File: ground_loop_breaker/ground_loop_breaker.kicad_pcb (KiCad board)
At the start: 2 copper layers, 72 parts, among them J1 Conn_01x02_Male, J10 Conn_01x02_Male, J11 Conn_Coaxial, J12 Conn_01x02_Male, J2 Conn_01x02_Male, J3 Conn_Coaxial, J4 Conn_01x02_Male, J5 Conn_Coaxial, J6 Conn_01x02_Male, J7 Conn_01x02_Male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

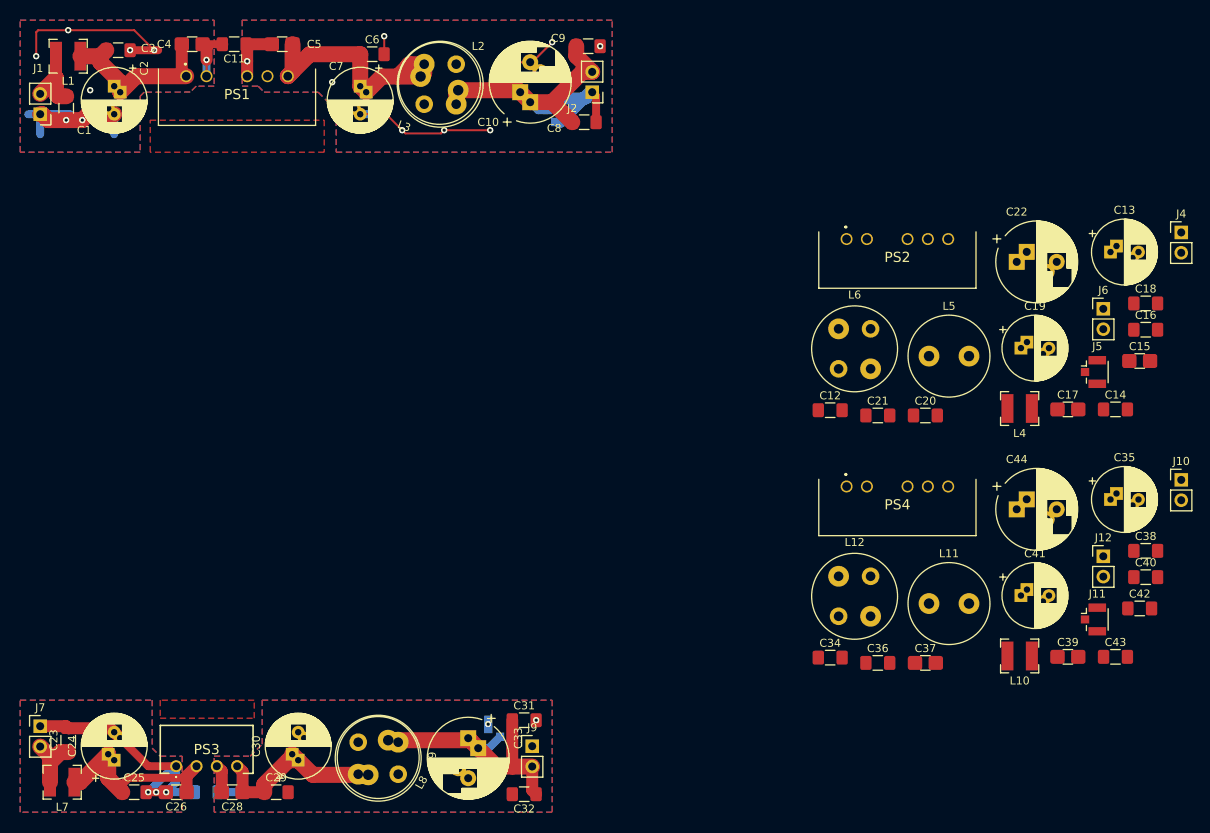
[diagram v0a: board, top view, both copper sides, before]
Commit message: ground loop breaker fin
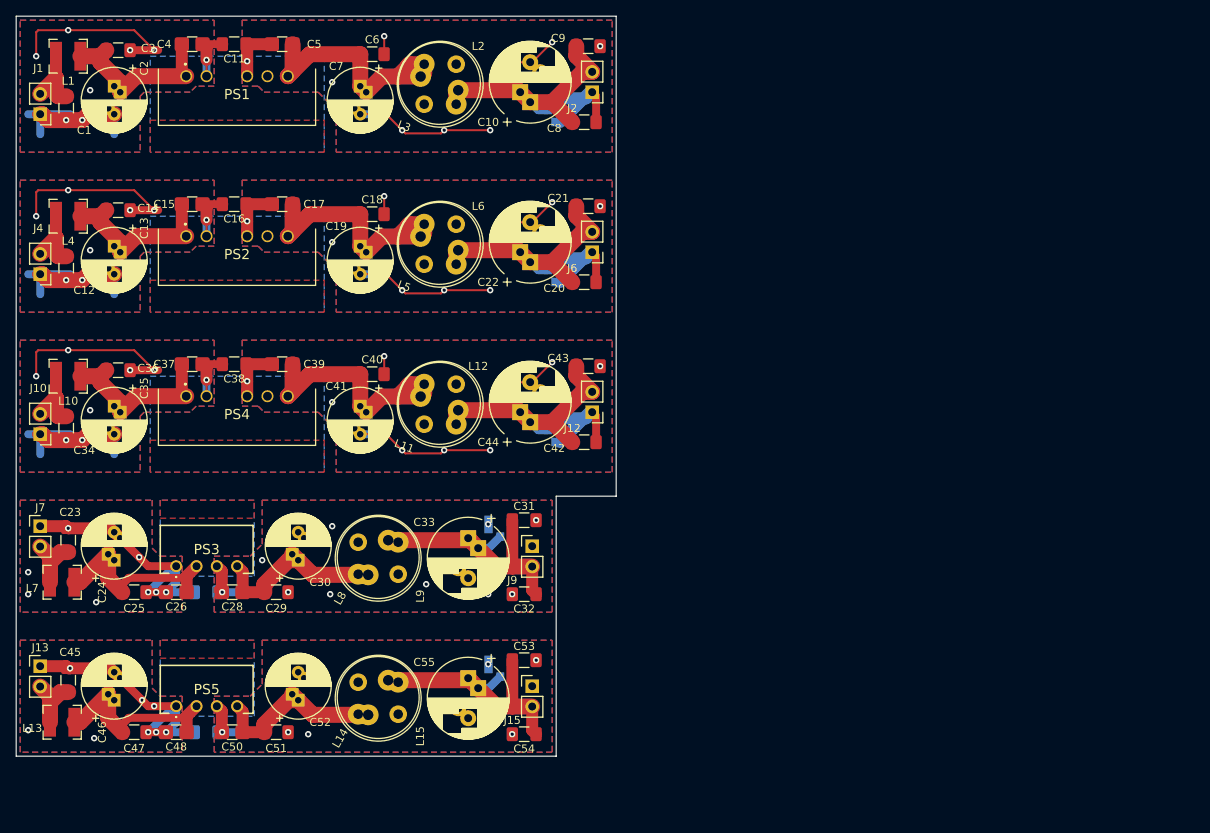
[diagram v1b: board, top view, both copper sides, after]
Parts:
- added C45: C, Capacitor_SMD:C_1206_3216Metric_Pad1.42x1.75mm_HandSolder, F.Cu at (81.5, 133.0)
- added C46: CP, SamacSys_Parts:CP_Radial_D8_P3.5_2.5, F.Cu at (87.2, 135.5)
- added C47: C, Capacitor_SMD:C_1206_3216Metric_Pad1.42x1.75mm_HandSolder, F.Cu at (89.8, 139.5)
- added C48: C, SamacSys_Parts:C_1206_0805_dual, F.Cu at (95.0, 139.5)
- added C49: 270p 1kV, Capacitor_SMD:C_1206_3216Metric_Pad1.42x1.75mm_HandSolder, B.Cu at (98.8, 139.5)
- added C50: C, SamacSys_Parts:C_1206_0805_dual, F.Cu at (102.0, 139.5)
- added C51: C, Capacitor_SMD:C_1206_3216Metric_Pad1.42x1.75mm_HandSolder, F.Cu at (107.5, 139.5)
- added C52: CP, SamacSys_Parts:CP_Radial_D8_P3.5_2.5, F.Cu at (110.2, 135.5)
- added C53: C, Capacitor_SMD:C_1206_3216Metric_Pad1.42x1.75mm_HandSolder, F.Cu at (138.5, 130.5)
- added C54: C, Capacitor_SMD:C_1206_3216Metric_Pad1.42x1.75mm_HandSolder, F.Cu at (138.5, 139.8)
- added C55: CP, SamacSys_Parts:CP_Radial_D10.0mm_P3.5_5, F.Cu at (131.5, 132.8)
- added J13: Conn_01x02_Male, Connector_PinHeader_2.54mm:PinHeader_1x02_P2.54mm_Vertical, F.Cu at (78.0, 131.2)
- added J14: Conn_Coaxial, Connector_Coaxial:U.FL_Hirose_U.FL-R-SMT-1_Vertical, B.Cu at (135.5, 131.5)
- added J15: Conn_01x02_Male, Connector_PinHeader_2.54mm:PinHeader_1x02_P2.54mm_Vertical, F.Cu at (139.5, 133.8)
- added L13: L, Inductor_SMD:L_Bourns-SRN4018, F.Cu at (80.8, 138.2)
- added L14: 12RS105C, Inductor_THT:L_Radial_D10.0mm_P5.00mm_Fastron_07P, F.Cu at (121.5, 133.0)
- added L15: 12RS105C, Inductor_THT:L_Radial_D10.5mm_P4.00x5.00mm_Murata_1200RS, F.Cu at (122.8, 133.2)
- added PS5: PDSE1-S5-S5-S, SamacSys_Parts:PDSE1S5S5S, F.Cu at (95.0, 136.2)
- J11, J5: moved to B.Cu
- moved J10 142.7 mm to (78.0, 102.2), turned to 180 degrees
- moved J4 142.7 mm to (78.0, 82.2), turned to 180 degrees
- moved C14 127.1 mm to (87.8, 74.2)
- moved C35 125.1 mm to (87.2, 98.8), turned to 270 degrees
- moved C13 124.5 mm to (87.2, 78.8), turned to 270 degrees
- moved L10 124.0 mm to (81.5, 95.0)
- moved L4 121.3 mm to (81.5, 75.0)
- moved C15 120.1 mm to (97.0, 73.5)
- moved C38 116.3 mm to (102.2, 93.5), turned to 180 degrees
- moved C16 115.0 mm to (102.2, 73.5), turned to 180 degrees
- moved C39 104.8 mm to (108.2, 93.5), turned to 180 degrees
- moved C36 101.8 mm to (87.8, 94.2)
- moved C17 101.5 mm to (108.2, 73.5), turned to 180 degrees
- moved C40 100.0 mm to (119.5, 94.8)
- moved C34 99.7 mm to (81.2, 101.5), turned to 270 degrees
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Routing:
- net /sheet61358710/VinN: track 0.00 -> 55.2 mm, vias 0 -> 8
- net /sheet613586DC/VinN: track 0.00 -> 55.2 mm, vias 0 -> 8
- net /sheet61358710/VoutN: track 0.00 -> 52.5 mm, vias 0 -> 9
- net /sheet613586DC/VoutN: track 0.00 -> 52.5 mm, vias 0 -> 9
- net /sheet61365BC2/VinN: track 0.00 -> 33.7 mm, vias 0 -> 9
- net /sheet61365BC2/VoutP: track 0.00 -> 33.5 mm
- net Net-(C39-Pad1): track 0.00 -> 32.8 mm
- net Net-(C17-Pad1): track 0.00 -> 32.8 mm
- net /sheet61358710/VoutP: track 0.00 -> 31.0 mm
- net /sheet613586DC/VoutP: track 0.00 -> 31.0 mm
- net Net-(C50-Pad1): track 0.00 -> 24.8 mm
- net Net-(C46-Pad1): track 0.00 -> 24.4 mm
- net Net-(C35-Pad1): track 0.00 -> 22.4 mm
- net Net-(C13-Pad1): track 0.00 -> 22.4 mm
- net /sheet61358710/VinP: track 0.00 -> 8.90 mm
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- added copper zone on B.Cu, net (none)
- added copper zone on B.Cu, net /sheet613586DC/VinN
- added copper zone on F.Cu, net /sheet613586DC/VinN
- added copper zone on B.Cu, net /sheet613586DC/VoutN
- added copper zone on F.Cu, net /sheet613586DC/VoutN
- added copper zone on B.Cu, net /sheet61358710/VinN
- added copper zone on F.Cu, net /sheet61358710/VinN
- added copper zone on B.Cu, net /sheet61358710/VoutN
- added copper zone on F.Cu, net /sheet61358710/VoutN
- added copper zone on B.Cu, net /sheet61365BC2/VinN
- added copper zone on F.Cu, net /sheet61365BC2/VinN
- added copper zone on B.Cu, net /sheet61365BC2/VoutN
- added copper zone on F.Cu, net /sheet61365BC2/VoutN
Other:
- board outline added: 75 x 92.5 mm
